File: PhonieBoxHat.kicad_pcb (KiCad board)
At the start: 2 copper layers, 65 x 56 mm, 33 parts, among them J1 Raspberry_Pi_2_3, J2 Display, J3 OnOffShim, J4 VOL-, J5 VOL+, J6 Prev, J7 Play/Pause, J8 Next, J9 PowerLed

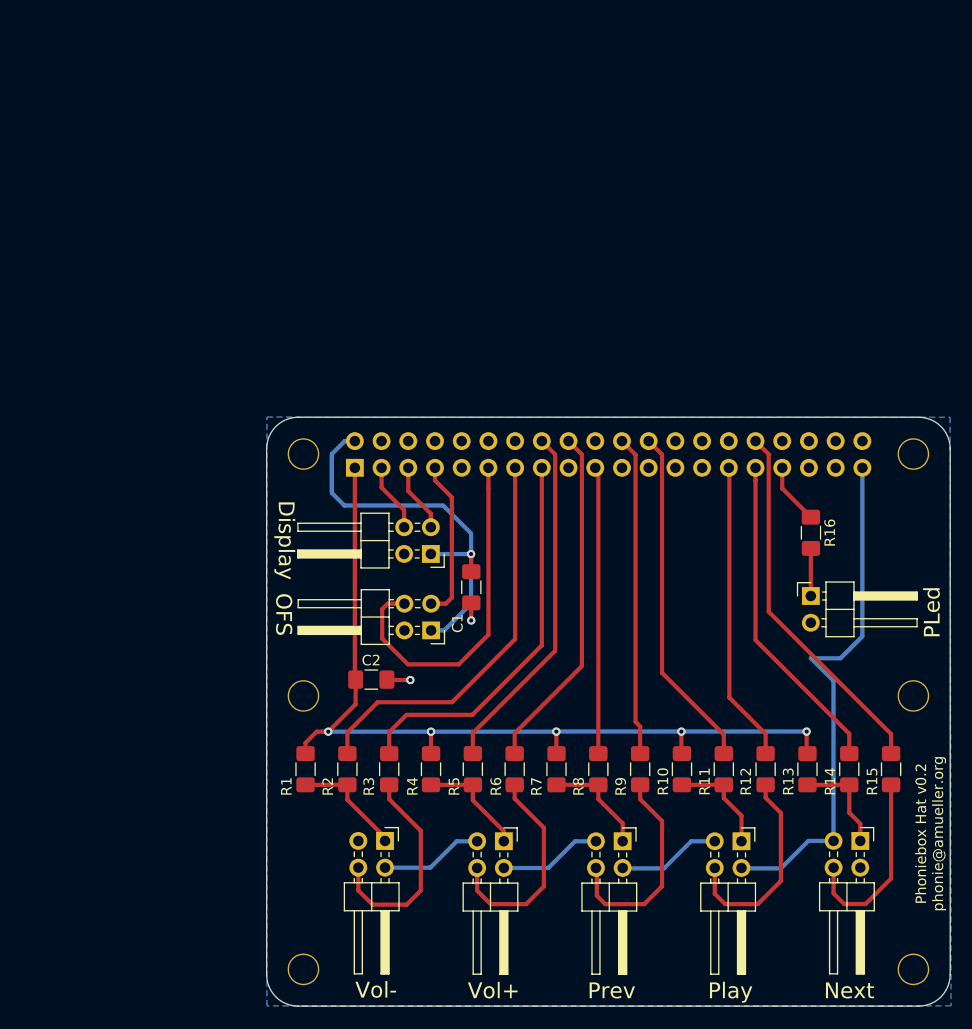
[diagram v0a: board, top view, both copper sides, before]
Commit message: v0.3
New version of the PCB to integrate the OnOffShim
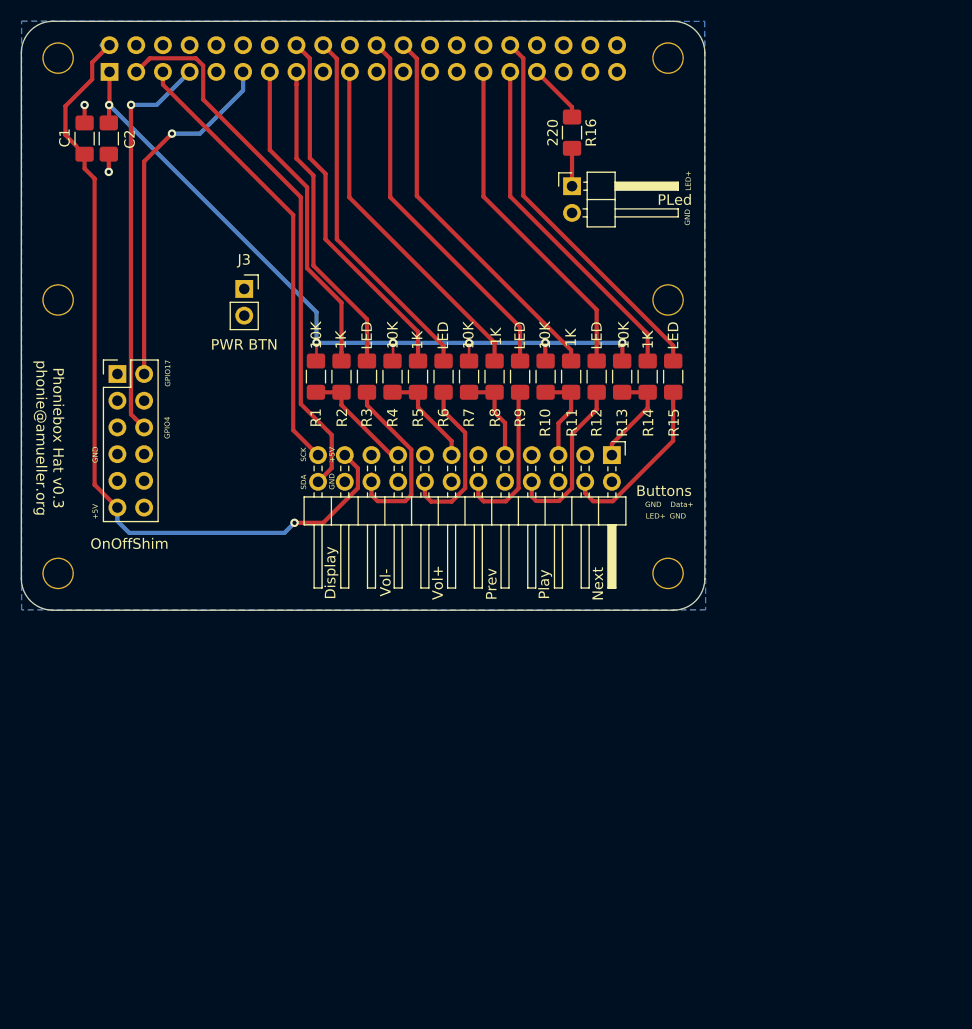
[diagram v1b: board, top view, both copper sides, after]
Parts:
- removed J4: VOL-, Connector_PinHeader_2.54mm:PinHeader_2x02_P2.54mm_Horizontal
- removed J5: VOL+, Connector_PinHeader_2.54mm:PinHeader_2x02_P2.54mm_Horizontal
- removed J6: Prev, Connector_PinHeader_2.54mm:PinHeader_2x02_P2.54mm_Horizontal
- removed J7: Play/Pause, Connector_PinHeader_2.54mm:PinHeader_2x02_P2.54mm_Horizontal
- removed J8: Next, Connector_PinHeader_2.54mm:PinHeader_2x02_P2.54mm_Horizontal
- added J10: Buttons, Connector_PinHeader_2.54mm:PinHeader_2x12_P2.54mm_Horizontal, F.Cu at (92.8, 93.6)
- J2: value Display -> OnOffShim; footprint Connector_PinHeader_2.54mm:PinHeader_2x02_P2.54mm_Horizontal -> Connector_PinHeader_2.54mm:PinHeader_2x06_P2.54mm_Vertical
- J3: value OnOffShim -> PWR BTN; footprint Connector_PinHeader_2.54mm:PinHeader_2x02_P2.54mm_Horizontal -> Connector_PinSocket_2.54mm:PinSocket_1x02_P2.54mm_Vertical
- R12, R15, R3, R6, R9: value 220 -> LED
- moved C2 57.2 mm to (45.0, 63.5), turned to 270 degrees
- moved C1 56.3 mm to (42.7, 63.5), turned to 270 degrees
- moved J9 45.1 mm to (89.0, 68.0)
- moved R16 44.3 mm to (89.0, 62.9)
- moved H1 44.3 mm to (40.2, 104.8)
- moved H4 44.3 mm to (98.2, 104.8)
- moved H5 44.3 mm to (98.2, 78.8)
- moved H6 44.3 mm to (40.2, 78.8)
- moved J1 44.3 mm to (45.1, 57.2)
- moved H2 44.3 mm to (40.2, 55.9)
- moved H3 44.3 mm to (98.2, 55.9)
- moved R15 42.7 mm to (98.7, 86.1)
- moved R14 42.0 mm to (96.2, 86.1), turned to 270 degrees
- moved R13 41.3 mm to (93.8, 86.1)
- moved R12 40.6 mm to (91.4, 86.1)
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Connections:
- J1 pad 10: Net-(J1-Pad10) -> (no net)
- J1 pad 12: Net-(J1-Pad12) -> (no net)
- J1 pad 14: Net-(J1-Pad14) -> (no net)
- J1 pad 17: Net-(J1-Pad17) -> (no net)
- J1 pad 20: Net-(J1-Pad20) -> (no net)
- J1 pad 21: Net-(J1-Pad21) -> (no net)
- J1 pad 23: Net-(J1-Pad23) -> (no net)
- J1 pad 25: Net-(J1-Pad25) -> (no net)
- J1 pad 26: Net-(J1-Pad26) -> (no net)
- J1 pad 27: Net-(J1-Pad27) -> (no net)
- J1 pad 28: Net-(J1-Pad28) -> (no net)
- J1 pad 30: Net-(J1-Pad30) -> (no net)
- J1 pad 34: Net-(J1-Pad34) -> (no net)
- J1 pad 35: Net-(J1-Pad35) -> (no net)
- J1 pad 36: Net-(J1-Pad36) -> (no net)
- J1 pad 37: Net-(J1-Pad37) -> (no net)
- J1 pad 38: Net-(J1-Pad38) -> (no net)
- J1 pad 4: Net-(J1-Pad4) -> (no net)
- J1 pad 40: Net-(J1-Pad40) -> (no net)
- J1 pad 6: Net-(J1-Pad6) -> (no net)
- J1 pad 8: Net-(J1-Pad8) -> (no net)
- J1 pad 9: Net-(J1-Pad9) -> (no net)
- J2 pad 1: +5V -> (no net)
- J2 pad 2: /GND -> /OFS2
- J2 pad 3: /Display1 -> (no net)
- J2 pad 4: /Display2 -> (no net)
- J3 pad 1: +5V -> (no net)
- J3 pad 2: /GND -> (no net)
- R1 pad 2: Net-(J4-Pad1) -> Net-(J10-Pad17)
- R10 pad 2: Net-(J7-Pad1) -> Net-(J10-Pad5)
- R11 pad 1: Net-(J7-Pad1) -> /PlayData
- R11 pad 2: /PlayData -> Net-(J10-Pad5)
- R13 pad 2: Net-(J8-Pad1) -> Net-(J10-Pad1)
- R14 pad 1: Net-(J8-Pad1) -> /NextData
- R14 pad 2: /NextData -> Net-(J10-Pad1)
- R2 pad 1: Net-(J4-Pad1) -> /Vol-Data
- R2 pad 2: /Vol-Data -> Net-(J10-Pad17)
- R7 pad 2: Net-(J6-Pad1) -> Net-(J10-Pad9)
- R8 pad 1: Net-(J6-Pad1) -> /PrevData
- R8 pad 2: /PrevData -> Net-(J10-Pad9)
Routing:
- net /GND: track 83.5 -> 3.54 mm
- net /Display2: track 6.58 -> 52.4 mm
- net +5V: track 39.4 -> 78.9 mm
- net /Display1: track 6.54 -> 42.5 mm
- net /OFS1: track 15.2 -> 38.1 mm, vias 0 -> 1
- net Net-(J4-Pad1): track 11.5 -> 0.00 mm
- net Net-(J8-Pad1): track 11.2 -> 0.00 mm
- net Net-(J10-Pad17): track 0.00 -> 11.0 mm
- net Net-(J6-Pad1): track 10.3 -> 0.00 mm
- net Net-(J7-Pad1): track 10.0 -> 0.00 mm
- net +3V3: track 83.7 -> 73.9 mm, vias 5 -> 6
- net Net-(J10-Pad1): track 0.00 -> 9.81 mm
- net Net-(J10-Pad5): track 0.00 -> 8.90 mm
- net Net-(J10-Pad9): track 0.00 -> 8.81 mm
- net /Vol-Data: track 37.9 -> 30.3 mm
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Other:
- board text added: "+5V"
- board text added: "Data+"
- board text added: "GND"
- board text added: "GPIO17"
- board text added: "GPIO4"
- board text added: "LED+"
- board text added: "Phoniebox Hat v0.3 phonie@amueller.org"
- board text added: "SCK"
- board text added: "SDA"
- board text removed: "OFS"
- board text removed: "Phoniebox Hat v0.2 phonie@amueller.org"
